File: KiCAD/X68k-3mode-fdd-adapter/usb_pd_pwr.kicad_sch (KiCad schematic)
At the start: 29 parts, among them J1001 Barrel_Jack_Switch, J1002 USB_C_Receptacle_USB2.0_14P, Q1001 FDS4935A, Q1002 FDS4935A, Q1003 FDS4935A, U1001 K7805M-1000R3, U1002 MCP1792x-5002xCB

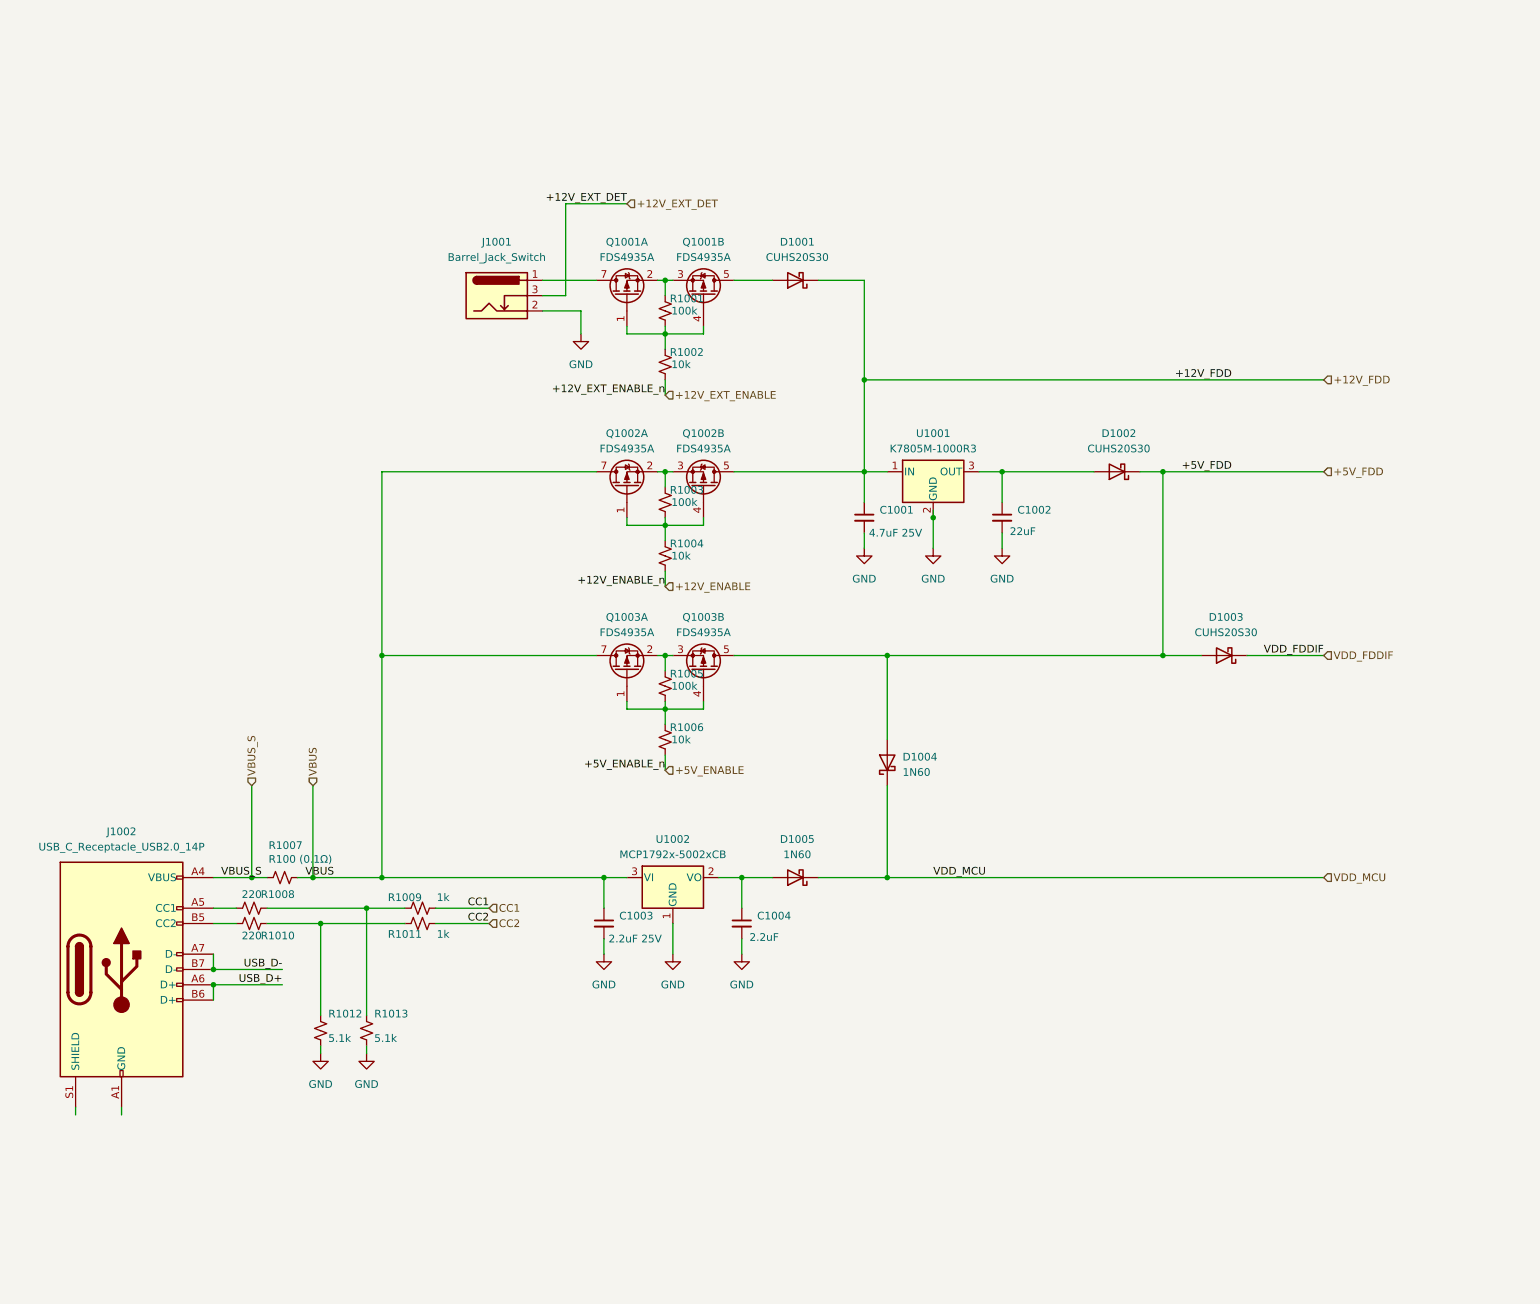
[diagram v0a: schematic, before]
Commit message: DRCエラー修正
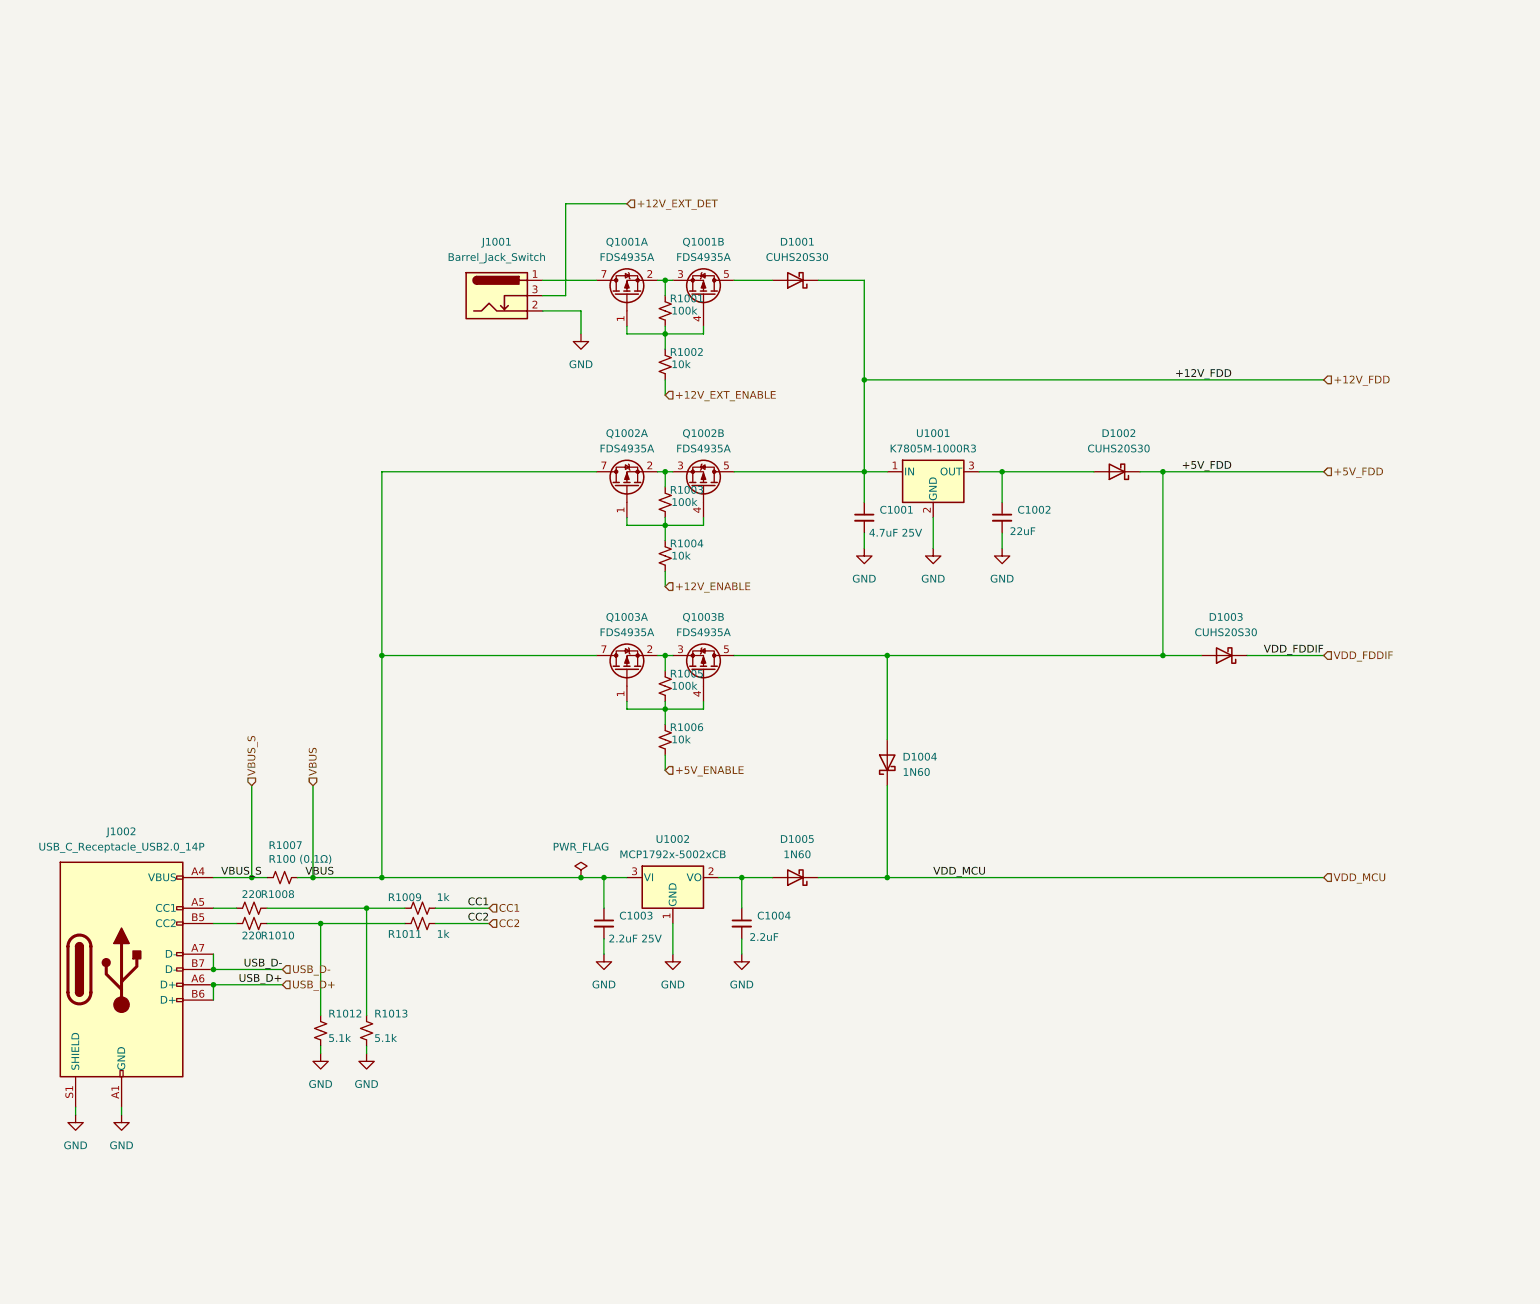
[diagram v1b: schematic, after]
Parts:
- Q1001, Q1002, Q1003: symbol X68k-lib:FDS4935A -> x68000-ext:FDS4935A
- U1001: symbol X68k-lib:K7805M-1000R3 -> x68000-ext:K7805M-1000R3
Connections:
- net GND: now also J1002.A1 (GND), J1002.A12 (GND), J1002.B1 (GND), J1002.B12 (GND), J1002.S1 (SHIELD)
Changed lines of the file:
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@@
 	)
 	(junction
+		(at 156.21 180.34)
+		(diameter 0)
+		(color 0 0 0 0)
+	)
+	(junction
 		(at 101.6 180.34)
 		(diameter 0)
@@
 	)
 	(junction
-		(at 214.63 120.65)
-		(diameter 0)
-		(color 0 0 0 0)
-	)
-	(junction
 		(at 111.76 180.34)
 		(diameter 0)
@@
 	(wire
 		(pts
-			(xy 123.19 180.34) (xy 160.02 180.34)
+			(xy 123.19 180.34) (xy 156.21 180.34)
 		)
 		(stroke
@@
 	(wire
 		(pts
-			(xy 214.63 119.38) (xy 214.63 120.65)
-		)
-		(stroke
-			(width 0)
-			(type default)
-		)
-	)
-	(wire
-		(pts
 			(xy 176.53 88.9) (xy 176.53 90.17)
 		)
@@
 	(wire
 		(pts
+			(xy 156.21 180.34) (xy 160.02 180.34)
+		)
+		(stroke
+			(width 0)
+			(type default)
+		)
+	)
+	(wire
+		(pts
 			(xy 181.61 81.28) (xy 187.96 81.28)
 		)
@@
 		)
 	)
-	(label "+5V_ENABLE_n"
-		(at 170.18 162.56 180)
-		(effects
-			(font
-				(size 1.27 1.27)
-			)
-			(justify right bottom)
-		)
-	)
 	(label "+12V_FDD"
 		(at 264.16 97.79 180)
@@
 		)
 	)
-	(label "+12V_EXT_ENABLE_n"
-		(at 170.18 100.33 180)
-		(effects
-			(font
-				(size 1.27 1.27)
-			)
-			(justify right bottom)
-		)
-	)
 	(label "CC1"
 		(at 140.97 185.42 180)
@@
 		)
 	)
-	(label "+12V_ENABLE_n"
-		(at 170.18 132.08 180)
-		(effects
-			(font
-				(size 1.27 1.27)
-			)
-			(justify right bottom)
-		)
-	)
-	(label "+12V_EXT_DET"
-		(at 163.83 68.58 180)
+	(hierarchical_label "USB_D+"
+		(shape input)
+		(at 106.68 198.12 0)
 		(effects
 			(font
 				(size 1.27 1.27)
 			)
-			(justify right bottom)
+			(justify left)
 		)
 	)
@@
 		)
 	)
+	(hierarchical_label "USB_D-"
+		(shape input)
+		(at 106.68 195.58 0)
+		(effects
+			(font
+				(size 1.27 1.27)
+			)
+			(justify left)
+		)
+	)
 	(hierarchical_label "CC2"
 		(shape input)
@@
 	)
 	(symbol
-		(lib_id "X68k-lib:K7805M-1000R3")
+		(lib_id "x68000-ext:K7805M-1000R3")
 		(at 214.63 113.03 0)
 		(unit 1)
@@
 	)
 	(symbol
+		(lib_id "power:GND")
+		(at 72.39 219.71 0)
+		(unit 1)
+		(exclude_from_sim no)
+		(in_bom yes)
+		(on_board yes)
+		(dnp no)
+		(fields_autoplaced yes)
+		(property "Reference" "#PWR01011"
+			(at 72.39 226.06 0)
+			(effects
+				(font
+					(size 1.27 1.27)
+				)
+				(hide yes)
+			)
+		)
+		(property "Value" "GND"
+			(at 72.39 224.79 0)
+			(effects
+				(font
+					(size 1.27 1.27)
+				)
+			)
+		)
+		(property "Footprint" ""
+			(at 72.39 219.71 0)
+			(effects
+				(font
+					(size 1.27 1.27)
+				)
+				(hide yes)
+			)
+		)
+		(property "Datasheet" ""
+			(at 72.39 219.71 0)
+			(effects
+				(font
+					(size 1.27 1.27)
+				)
+				(hide yes)
+			)
+		)
+		(property "Description" "Power symbol creates a global label with name \"GND\" , ground"
+			(at 72.39 219.71 0)
+			(effects
+				(font
+					(size 1.27 1.27)
+				)
+				(hide yes)
+			)
+		)
+		(pin "1"
+		)
+		(instances
+			(project "X68k-3mode-fdd-adapter"
+				(path "/13b3a4ee-84d6-44b3-962d-9cf7c36d7564/e2bad364-aaa3-4f08-8f3b-45fc5db28f5a"
+					(reference "#PWR01011")
+					(unit 1)
+				)
+			)
+		)
+	)
+	(symbol
 		(lib_id "Device:R_Small_US")
 		(at 120.65 205.74 0)
@@
 	)
 	(symbol
+		(lib_id "power:PWR_FLAG")
+		(at 156.21 180.34 0)
+		(unit 1)
+		(exclude_from_sim no)
+		(in_bom yes)
+		(on_board yes)
+		(dnp no)
+		(fields_autoplaced yes)
+		(property "Reference" "#FLG01001"
+			(at 156.21 178.435 0)
+			(effects
+				(font
+					(size 1.27 1.27)
+				)
+				(hide yes)
+			)
+		)
+		(property "Value" "PWR_FLAG"
+			(at 156.21 175.26 0)
+			(effects
+				(font
+					(size 1.27 1.27)
+				)
+			)
+		)
+		(property "Footprint" ""
+			(at 156.21 180.34 0)
+			(effects
+				(font
+					(size 1.27 1.27)
+				)
+				(hide yes)
+			)
+		)
+		(property "Datasheet" "~"
+			(at 156.21 180.34 0)
+			(effects
+				(font
+					(size 1.27 1.27)
+				)
+				(hide yes)
+			)
+		)
+		(property "Description" "Special symbol for telling ERC where power comes from"
+			(at 156.21 180.34 0)
+			(effects
+				(font
+					(size 1.27 1.27)
+				)
+				(hide yes)
+			)
+		)
+		(pin "1"
+		)
+		(instances
+			(project ""
+				(path "/13b3a4ee-84d6-44b3-962d-9cf7c36d7564/e2bad364-aaa3-4f08-8f3b-45fc5db28f5a"
+					(reference "#FLG01001")
+					(unit 1)
+				)
+			)
+		)
+	)
+	(symbol
 		(lib_id "Device:C_Small")
 		(at 226.06 120.65 0)
@@
 	)
 	(symbol
-		(lib_id "X68k-lib:FDS4935A")
+		(lib_id "x68000-ext:FDS4935A")
 		(at 163.83 146.05 90)
 		(unit 1)
@@
 	)
 	(symbol
-		(lib_id "X68k-lib:FDS4935A")
+		(lib_id "x68000-ext:FDS4935A")
 		(at 176.53 115.57 270)
 		(mirror x)
@@
 	)
 	(symbol
+		(lib_id "power:GND")
+		(at 80.01 219.71 0)
+		(unit 1)
+		(exclude_from_sim no)
+		(in_bom yes)
+		(on_board yes)
+		(dnp no)
+		(fields_autoplaced yes)
+		(property "Reference" "#PWR01010"
+			(at 80.01 226.06 0)
+			(effects
+				(font
+					(size 1.27 1.27)
+				)
+				(hide yes)
+			)
+		)
+		(property "Value" "GND"
+			(at 80.01 224.79 0)
+			(effects
+				(font
+					(size 1.27 1.27)
+				)
+			)
+		)
+		(property "Footprint" ""
+			(at 80.01 219.71 0)
+			(effects
+				(font
+					(size 1.27 1.27)
+				)
+				(hide yes)
+			)
+		)
+		(property "Datasheet" ""
+			(at 80.01 219.71 0)
+			(effects
+				(font
+					(size 1.27 1.27)
+				)
+				(hide yes)
+			)
+		)
+		(property "Description" "Power symbol creates a global label with name \"GND\" , ground"
+			(at 80.01 219.71 0)
+			(effects
+				(font
+					(size 1.27 1.27)
+				)
+				(hide yes)
+			)
+		)
+		(pin "1"
+		)
+		(instances
+			(project "X68k-3mode-fdd-adapter"
+				(path "/13b3a4ee-84d6-44b3-962d-9cf7c36d7564/e2bad364-aaa3-4f08-8f3b-45fc5db28f5a"
+					(reference "#PWR01010")
+					(unit 1)
+				)
+			)
+		)
+	)
+	(symbol
 		(lib_id "Device:R_Small_US")
 		(at 170.18 86.36 0)
@@
 	)
 	(symbol
-		(lib_id "X68k-lib:FDS4935A")
+		(lib_id "x68000-ext:FDS4935A")
 		(at 163.83 115.57 90)
 		(unit 1)
@@
 	)
 	(symbol
-		(lib_id "X68k-lib:FDS4935A")
+		(lib_id "x68000-ext:FDS4935A")
 		(at 163.83 83.82 90)
 		(unit 1)
@@
 	)
 	(symbol
-		(lib_id "X68k-lib:FDS4935A")
+		(lib_id "x68000-ext:FDS4935A")
 		(at 176.53 146.05 270)
 		(mirror x)
@@
 	)
 	(symbol
-		(lib_id "X68k-lib:FDS4935A")
+		(lib_id "x68000-ext:FDS4935A")
 		(at 176.53 83.82 270)
 		(mirror x)

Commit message: フットプリントを一通り割り当てた
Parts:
- removed J1002: USB_C_Receptacle_USB2.0_14P, symbol Connector:USB_C_Receptacle_USB2.0_14P
- added J1003: USB_C_Receptacle_USB2.0_16P, Connector_USB:USB_C_Receptacle_G-Switch_GT-USB-7010ASV, symbol Connector:USB_C_Receptacle_USB2.0_16P
- C1001: value 4.7uF 25V -> 4.7uF 50V; footprint (none) -> Capacitor_SMD:C_1206_3216Metric_Pad1.33x1.80mm_HandSolder; LCSC (none) -> C51205
- C1002: value 22uF -> 22uF 25V; footprint (none) -> Capacitor_SMD:C_0805_2012Metric_Pad1.18x1.45mm_HandSolder; LCSC (none) -> C602037
- C1003: footprint (none) -> Capacitor_SMD:C_0805_2012Metric_Pad1.18x1.45mm_HandSolder; LCSC (none) -> C19110
- C1004: value 2.2uF -> 2.2uF 25V; footprint (none) -> Capacitor_SMD:C_0805_2012Metric_Pad1.18x1.45mm_HandSolder
- D1001, D1002, D1003: footprint (none) -> x68k-lib:CUHS20S30 (US2H)
- D1004, D1005: value 1N60 -> 1N60PW; footprint (none) -> Diode_SMD:D_SOD-123; LCSC C5636538 -> C134188
- J1001: footprint (none) -> Connector_BarrelJack:BarrelJack_Horizontal
- R1001, R1002, R1003, R1004, R1005, R1006, R1008, R1009, R1010, R1011, R1012, R1013: footprint (none) -> Resistor_SMD:R_0603_1608Metric
- U1001: footprint (none) -> Converter_DCDC:Converter_DCDC_RECOM_R-78E-0.5_THT
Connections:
- net GND: now also J1003.A1 (GND), J1003.A12 (GND), J1003.B1 (GND), J1003.B12 (GND), J1003.S1 (SHIELD)
- net USB_D+: now also J1003.A6 (D+), J1003.B6 (D+)
- net USB_D-: now also J1003.A7 (D-), J1003.B7 (D-)
- net VBUS_S: now also J1003.A4 (VBUS), J1003.A9 (VBUS), J1003.B4 (VBUS), J1003.B9 (VBUS)
- net at R1010.1: now also J1003.B5 (CC2)
- net at R1008.1: now also J1003.A5 (CC1)
- no-connect marks 0 -> 2

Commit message: PCBの配線完了
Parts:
- removed R1009, R1011: 1k, Resistor_SMD:R_0603_1608Metric, symbol Device:R_Small_US
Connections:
- net CC1: now also R1008.2, R1013.1
- net CC2: now also R1010.2, R1012.1
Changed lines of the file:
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@@
 	(wire
 		(pts
-			(xy 132.08 185.42) (xy 140.97 185.42)
-		)
-		(stroke
-			(width 0)
-			(type default)
-		)
-	)
-	(wire
-		(pts
 			(xy 163.83 152.4) (xy 170.18 152.4)
 		)
@@
 	(wire
 		(pts
-			(xy 132.08 187.96) (xy 140.97 187.96)
-		)
-		(stroke
-			(width 0)
-			(type default)
-		)
-	)
-	(wire
-		(pts
 			(xy 163.83 90.17) (xy 170.18 90.17)
 		)
@@
 	)
 	(label "CC1"
-		(at 140.97 185.42 180)
+		(at 127 185.42 180)
 		(effects
 			(font
@@
 	)
 	(label "CC2"
-		(at 140.97 187.96 180)
+		(at 127 187.96 180)
 		(effects
 			(font
@@
 	(hierarchical_label "CC1"
 		(shape input)
-		(at 140.97 185.42 0)
+		(at 127 185.42 0)
 		(effects
 			(font
@@
 	(hierarchical_label "CC2"
 		(shape input)
-		(at 140.97 187.96 0)
+		(at 127 187.96 0)
 		(effects
 			(font
@@
 	)
 	(symbol
-		(lib_id "Device:R_Small_US")
-		(at 129.54 187.96 90)
-		(unit 1)
-		(exclude_from_sim no)
-		(in_bom yes)
-		(on_board yes)
-		(dnp no)
-		(property "Reference" "R1011"
-			(at 127 189.738 90)
-			(effects
-				(font
-					(size 1.27 1.27)
-				)
-			)
-		)
-		(property "Value" "1k"
-			(at 133.35 189.738 90)
-			(effects
-				(font
-					(size 1.27 1.27)
-				)
-			)
-		)
-		(property "Footprint" "Resistor_SMD:R_0603_1608Metric"
-			(at 129.54 187.96 0)
-			(effects
-				(font
-					(size 1.27 1.27)
-				)
-				(hide yes)
-			)
-		)
-		(property "Datasheet" "~"
-			(at 129.54 187.96 0)
-			(effects
-				(font
-					(size 1.27 1.27)
-				)
-				(hide yes)
-			)
-		)
-		(property "Description" "Resistor, small US symbol"
-			(at 129.54 187.96 0)
-			(effects
-				(font
-					(size 1.27 1.27)
-				)
-				(hide yes)
-			)
-		)
-		(pin "2"
-		)
-		(pin "1"
-		)
-		(instances
-			(project "X68k-3mode-fdd-adapter"
-				(path "/13b3a4ee-84d6-44b3-962d-9cf7c36d7564/e2bad364-aaa3-4f08-8f3b-45fc5db28f5a"
-					(reference "R1011")
-					(unit 1)
-				)
-			)
-		)
-	)
-	(symbol
 		(lib_id "power:GND")
 		(at 156.21 90.17 0)
@@
 					(unit 1)
 				)
-			)
-		)
-	)
-	(symbol
-		(lib_id "Device:R_Small_US")
-		(at 129.54 185.42 90)
-		(unit 1)
-		(exclude_from_sim no)
-		(in_bom yes)
-		(on_board yes)
-		(dnp no)
-		(property "Reference" "R1009"
-			(at 127 183.642 90)
-			(effects
-				(font
-					(size 1.27 1.27)
-				)
-			)
-		)
-		(property "Value" "1k"
-			(at 133.35 183.642 90)
-			(effects
-				(font
-					(size 1.27 1.27)
-				)
-			)
-		)
-		(property "Footprint" "Resistor_SMD:R_0603_1608Metric"
-			(at 129.54 185.42 0)
-			(effects
-				(font
-					(size 1.27 1.27)
-				)
-				(hide yes)
-			)
-		)
-		(property "Datasheet" "~"
-			(at 129.54 185.42 0)
-			(effects
-				(font
-					(size 1.27 1.27)
-				)
-				(hide yes)
-			)
-		)
-		(property "Description" "Resistor, small US symbol"
-			(at 129.54 185.42 0)
-			(effects
-				(font
-					(size 1.27 1.27)
-				)
-				(hide yes)
-			)
-		)
-		(pin "2"
-		)
-		(pin "1"
-		)
-		(instances
-			(project "X68k-3mode-fdd-adapter"
-				(path "/13b3a4ee-84d6-44b3-962d-9cf7c36d7564/e2bad364-aaa3-4f08-8f3b-45fc5db28f5a"
-					(reference "R1009")
-					(unit 1)
-				)

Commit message: シルクをさらに調整
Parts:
- renumbered J1003 to J1002, R1010 to R1009, R1012 to R1010, R1013 to R1011
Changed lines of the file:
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@@
 		(on_board yes)
 		(dnp no)
-		(property "Reference" "R1013"
+		(property "Reference" "R1011"
 			(at 121.92 202.946 0)
 			(effects
@@
 			(project "X68k-3mode-fdd-adapter"
 				(path "/13b3a4ee-84d6-44b3-962d-9cf7c36d7564/e2bad364-aaa3-4f08-8f3b-45fc5db28f5a"
-					(reference "R1013")
+					(reference "R1011")
 					(unit 1)
 				)
@@
 		(on_board yes)
 		(dnp no)
-		(property "Reference" "R1010"
+		(property "Reference" "R1009"
 			(at 105.918 189.992 90)
 			(effects
@@
 			(project "X68k-3mode-fdd-adapter"
 				(path "/13b3a4ee-84d6-44b3-962d-9cf7c36d7564/e2bad364-aaa3-4f08-8f3b-45fc5db28f5a"
-					(reference "R1010")
+					(reference "R1009")
 					(unit 1)
 				)
@@
 		(on_board yes)
 		(dnp no)
-		(property "Reference" "R1012"
+		(property "Reference" "R1010"
 			(at 114.3 202.946 0)
 			(effects
@@
 			(project "X68k-3mode-fdd-adapter"
 				(path "/13b3a4ee-84d6-44b3-962d-9cf7c36d7564/e2bad364-aaa3-4f08-8f3b-45fc5db28f5a"
-					(reference "R1012")
+					(reference "R1010")
 					(unit 1)
 				)
@@
 		(dnp no)
 		(fields_autoplaced yes)
-		(property "Reference" "J1003"
+		(property "Reference" "J1002"
 			(at 80.01 172.72 0)
 			(effects
@@
 			(project ""
 				(path "/13b3a4ee-84d6-44b3-962d-9cf7c36d7564/e2bad364-aaa3-4f08-8f3b-45fc5db28f5a"
-					(reference "J1003")
-					(unit 1)
-				)
+					(reference "J1002")
+					(unit 1)
+				)

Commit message: v2.0.1向けの修正を一通り入れたので一旦コミット
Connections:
- net at Q1003.3 (S2), R1005.1: now also Q1003.1 (S2); no longer Q1003.2 (S2)
- net at Q1003.4 (G2), R1005.2, R1006.1: now also Q1003.2 (G2); no longer Q1003.1 (G2)
- net at Q1002.3 (S2), R1003.1: now also Q1002.1 (S2); no longer Q1002.2 (S2)
- net at Q1002.4 (G2), R1003.2, R1004.1: now also Q1002.2 (G2); no longer Q1002.1 (G2)
- net at Q1001.3 (S2), R1001.1: now also Q1001.1 (S2); no longer Q1001.2 (S2)
- net at Q1001.4 (G2), R1001.2, R1002.1: now also Q1001.2 (G2); no longer Q1001.1 (G2)
